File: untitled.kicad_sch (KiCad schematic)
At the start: 9 parts, among them J20 Conn_01x04_Socket, J21 Conn_01x02_Socket, U16 LTV-247

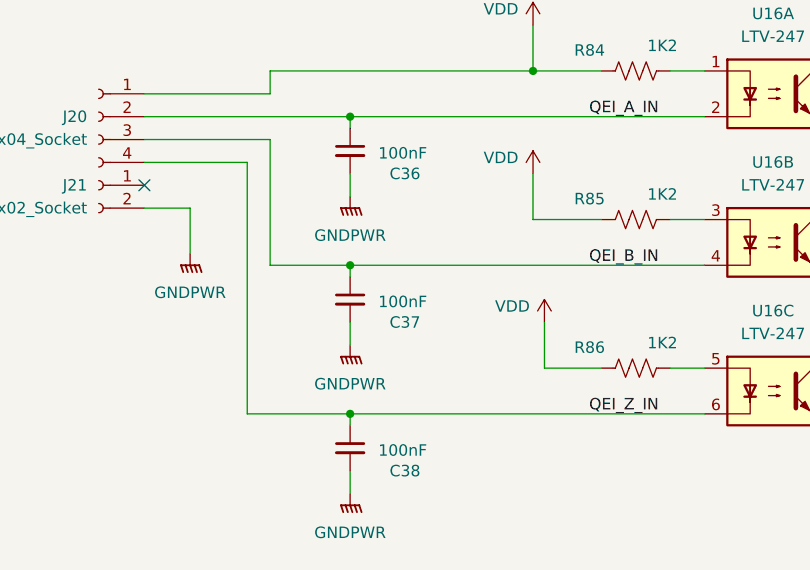
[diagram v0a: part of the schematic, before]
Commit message: Layout for stepper drivers and digital inputs
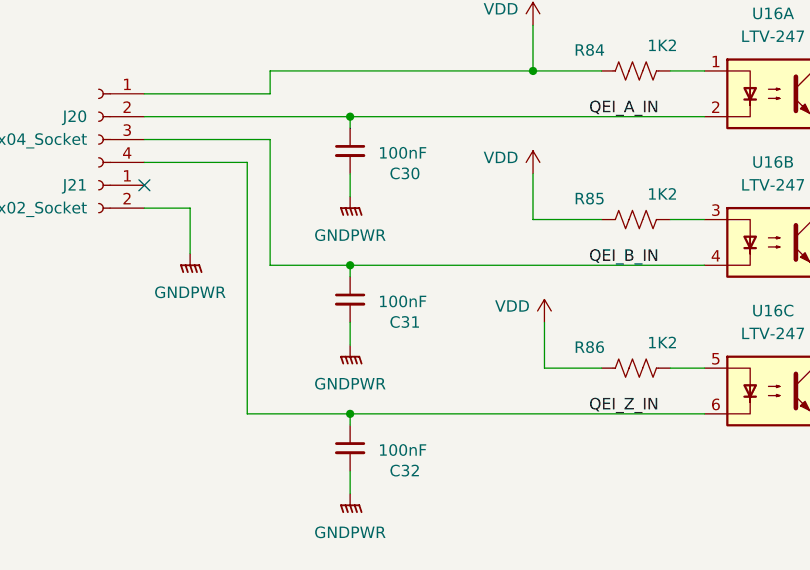
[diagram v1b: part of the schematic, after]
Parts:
- renumbered C36 to C30, C37 to C31, C38 to C32
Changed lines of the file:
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@@
 		(on_board yes)
 		(dnp no)
-		(property "Reference" "#PWR0228"
+		(property "Reference" "#PWR0203"
 			(at 138.43 73.66 0)
 			(effects
@@
 			(project "Remora Nucleo F446ZE Hat"
 				(path "/5473abc6-7b93-43cc-a401-f691c4d7d7cf/e401cb00-fa11-4a99-9e35-1d19f69fa4a0"
-					(reference "#PWR0228")
+					(reference "#PWR0203")
 					(unit 1)
 				)
@@
 		(on_board yes)
 		(dnp no)
-		(property "Reference" "C38"
+		(property "Reference" "C32"
 			(at 124.206 119.38 0)
 			(effects
@@
 			(project "Remora Nucleo F446ZE Hat"
 				(path "/5473abc6-7b93-43cc-a401-f691c4d7d7cf/e401cb00-fa11-4a99-9e35-1d19f69fa4a0"
-					(reference "C38")
+					(reference "C32")
 					(unit 1)
 				)
@@
 		(on_board yes)
 		(dnp no)
-		(property "Reference" "#PWR0229"
+		(property "Reference" "#PWR0204"
 			(at 138.43 90.17 0)
 			(effects
@@
 			(project "Remora Nucleo F446ZE Hat"
 				(path "/5473abc6-7b93-43cc-a401-f691c4d7d7cf/e401cb00-fa11-4a99-9e35-1d19f69fa4a0"
-					(reference "#PWR0229")
+					(reference "#PWR0204")
 					(unit 1)
 				)
@@
 		(on_board yes)
 		(dnp no)
-		(property "Reference" "C37"
+		(property "Reference" "C31"
 			(at 124.206 102.87 0)
 			(effects
@@
 			(project "Remora Nucleo F446ZE Hat"
 				(path "/5473abc6-7b93-43cc-a401-f691c4d7d7cf/e401cb00-fa11-4a99-9e35-1d19f69fa4a0"
-					(reference "C37")
+					(reference "C31")
 					(unit 1)
 				)
@@
 		(on_board yes)
 		(dnp no)
-		(property "Reference" "#PWR0230"
+		(property "Reference" "#PWR0205"
 			(at 139.7 106.68 0)
 			(effects
@@
 			(project "Remora Nucleo F446ZE Hat"
 				(path "/5473abc6-7b93-43cc-a401-f691c4d7d7cf/e401cb00-fa11-4a99-9e35-1d19f69fa4a0"
-					(reference "#PWR0230")
+					(reference "#PWR0205")
 					(unit 1)
 				)
@@
 		(on_board yes)
 		(dnp no)
-		(property "Reference" "C36"
+		(property "Reference" "C30"
 			(at 124.206 86.36 0)
 			(effects
@@
 			(project "Remora Nucleo F446ZE Hat"
 				(path "/5473abc6-7b93-43cc-a401-f691c4d7d7cf/e401cb00-fa11-4a99-9e35-1d19f69fa4a0"
-					(reference "C36")
+					(reference "C30")
 					(unit 1)
 				)
@@
 		(dnp no)
 		(fields_autoplaced yes)
-		(property "Reference" "#PWR0203"
+		(property "Reference" "#PWR0206"
 			(at 193.04 128.27 0)
 			(effects
@@
 			(project "Remora Nucleo F446ZE Hat"
 				(path "/5473abc6-7b93-43cc-a401-f691c4d7d7cf/e401cb00-fa11-4a99-9e35-1d19f69fa4a0"
-					(reference "#PWR0203")
-					(unit 1)
-				)
+					(reference "#PWR0206")
+					(unit 1)
+				)

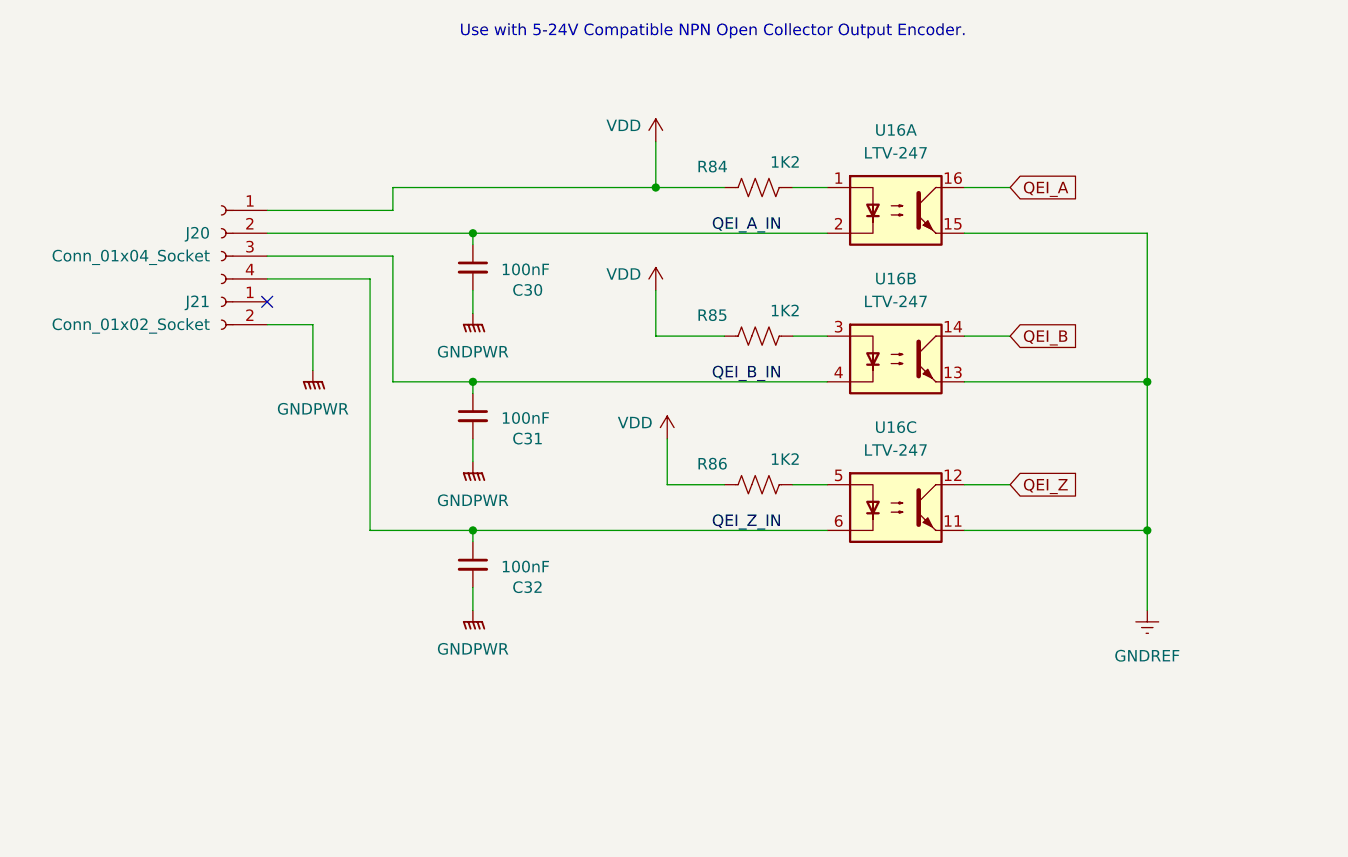
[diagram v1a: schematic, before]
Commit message: Switched terminal footprints over to a finer pitch. Corrected an issue with component reference values preventing proper use of multi channel rule areas. Component references for 4 channel optos are more straightforward as a result
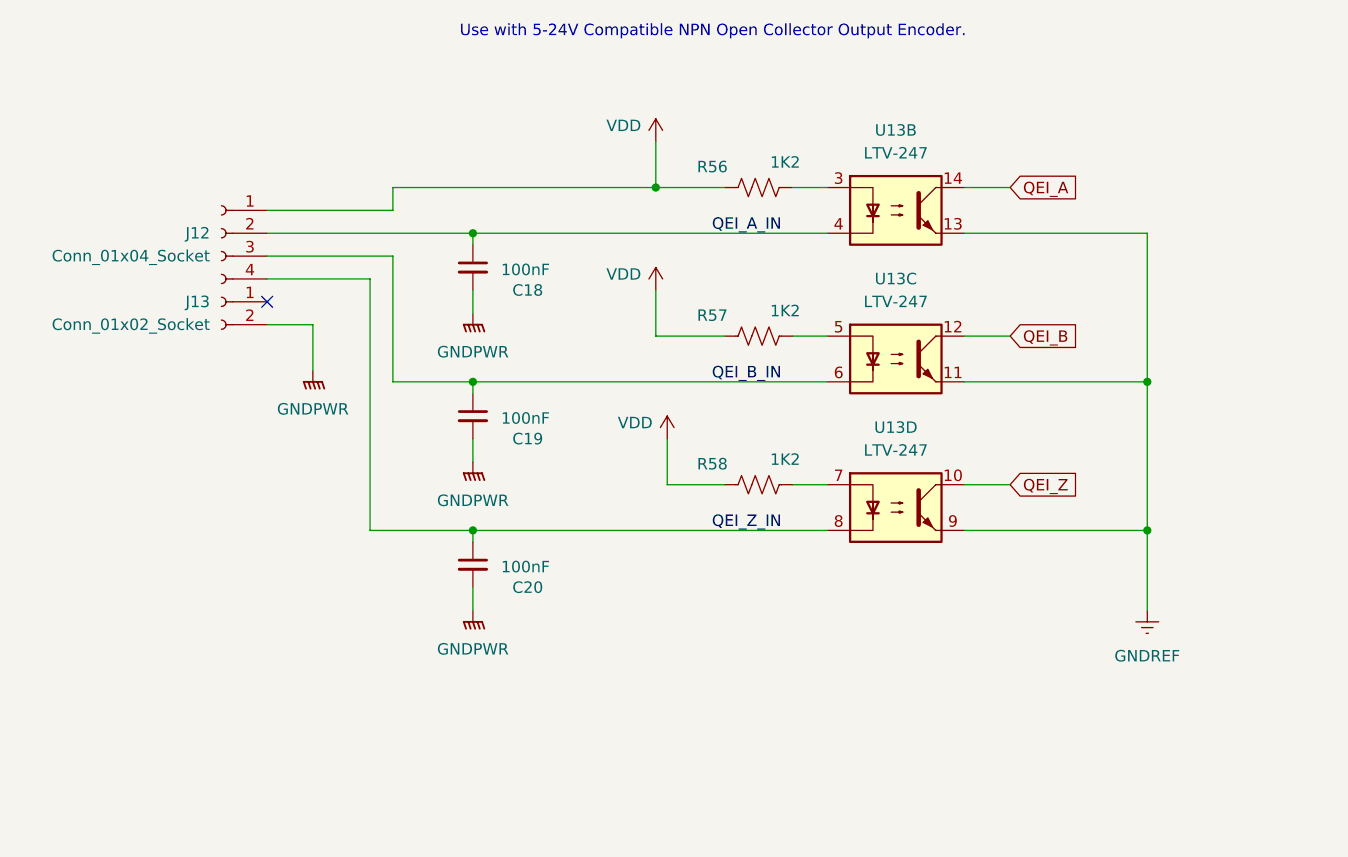
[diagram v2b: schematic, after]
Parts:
- removed U16: LTV-247, Package_SO:SOP-16_4.4x10.4mm_P1.27mm, symbol Isolator:LTV-247
- added U13: LTV-247, Package_SO:SOP-16_4.4x10.4mm_P1.27mm, symbol Isolator:LTV-247
- J12: renamed from J20; footprint Amphenol QT:QT04ADP83V0000G -> 691412120004B:691412120004B; Digikey Part Number 1818-QT04ADP83V0000G-ND -> 732-691412120004B-ND; Digikey URL https://www.digikey.com.au/en/products/detail/amphenol-anyt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 -> https://www.digikey.com.au/en/products/detail/w%C3%BCrth-el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
- J13: renamed from J21; footprint Amphenol QT:QT02ADP83V0000G -> 691412120002B:691412120002B; Digikey Part Number 1818-QT02ADP83V0000G-ND -> 732-691412120002B-ND; Digikey URL https://www.digikey.com.au/en/products/detail/amphenol-anyt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 -> https://www.digikey.com.au/en/products/detail/w%C3%BCrth-el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
- renumbered C30 to C18, C31 to C19, C32 to C20, R84 to R56, R85 to R57, R86 to R58
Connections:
- net GNDREF: now also U13.11, U13.13, U13.9
- net QEI_A: now also U13.14
- net QEI_A_IN: now also U13.4
- net QEI_B: now also U13.12
- net QEI_B_IN: now also U13.6
- net QEI_Z: now also U13.10
- net QEI_Z_IN: now also U13.8
- net at R57.1: now also U13.5
- net at R58.1: now also U13.7
- net at R56.1: now also U13.3

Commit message: Added 3d Models for new terminal connectors for easy board verification before committing to build
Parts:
- renumbered C18 to C30, C19 to C31, C20 to C32, J12 to J20, J13 to J21, R56 to R88, R57 to R89, R58 to R90, U13 to U17
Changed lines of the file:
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@@
 		(dnp no)
 		(fields_autoplaced yes)
-		(property "Reference" "J12"
+		(property "Reference" "J20"
 			(at 88.9 80.0099 0)
 			(effects
@@
 			(project "Remora Nucleo F446ZE Hat"
 				(path "/5473abc6-7b93-43cc-a401-f691c4d7d7cf/e401cb00-fa11-4a99-9e35-1d19f69fa4a0"
-					(reference "J12")
+					(reference "J20")
 					(unit 1)
 				)
@@
 		(on_board yes)
 		(dnp no)
-		(property "Reference" "R58"
+		(property "Reference" "R90"
 			(at 143.002 105.664 90)
 			(effects
@@
 			(project "Remora Nucleo F446ZE Hat"
 				(path "/5473abc6-7b93-43cc-a401-f691c4d7d7cf/e401cb00-fa11-4a99-9e35-1d19f69fa4a0"
-					(reference "R58")
+					(reference "R90")
 					(unit 1)
 				)
@@
 		(dnp no)
 		(fields_autoplaced yes)
-		(property "Reference" "U13"
+		(property "Reference" "U17"
 			(at 165.1 68.58 0)
 			(effects
@@
 			(project "Remora Nucleo F446ZE Hat"
 				(path "/5473abc6-7b93-43cc-a401-f691c4d7d7cf/e401cb00-fa11-4a99-9e35-1d19f69fa4a0"
-					(reference "U13")
+					(reference "U17")
 					(unit 2)
 				)
@@
 		(on_board yes)
 		(dnp no)
-		(property "Reference" "#PWR0143"
+		(property "Reference" "#PWR0211"
 			(at 138.43 73.66 0)
 			(effects
@@
 			(project "Remora Nucleo F446ZE Hat"
 				(path "/5473abc6-7b93-43cc-a401-f691c4d7d7cf/e401cb00-fa11-4a99-9e35-1d19f69fa4a0"
-					(reference "#PWR0143")
+					(reference "#PWR0211")
 					(unit 1)
 				)
@@
 		(on_board yes)
 		(dnp no)
-		(property "Reference" "C20"
+		(property "Reference" "C32"
 			(at 124.206 119.38 0)
 			(effects
@@
 			(project "Remora Nucleo F446ZE Hat"
 				(path "/5473abc6-7b93-43cc-a401-f691c4d7d7cf/e401cb00-fa11-4a99-9e35-1d19f69fa4a0"
-					(reference "C20")
+					(reference "C32")
 					(unit 1)
 				)
@@
 		(dnp no)
 		(fields_autoplaced yes)
-		(property "Reference" "J13"
+		(property "Reference" "J21"
 			(at 88.9 87.6299 0)
 			(effects
@@
 			(project "Remora Nucleo F446ZE Hat"
 				(path "/5473abc6-7b93-43cc-a401-f691c4d7d7cf/e401cb00-fa11-4a99-9e35-1d19f69fa4a0"
-					(reference "J13")
+					(reference "J21")
 					(unit 1)
 				)
@@
 		(on_board yes)
 		(dnp no)
-		(property "Reference" "#PWR0144"
+		(property "Reference" "#PWR0212"
 			(at 138.43 90.17 0)
 			(effects
@@
 			(project "Remora Nucleo F446ZE Hat"
 				(path "/5473abc6-7b93-43cc-a401-f691c4d7d7cf/e401cb00-fa11-4a99-9e35-1d19f69fa4a0"
-					(reference "#PWR0144")
+					(reference "#PWR0212")
 					(unit 1)
 				)
@@
 		(on_board no)
 		(dnp no)
-		(property "Reference" "#PWR0140"
+		(property "Reference" "#PWR0208"
 			(at 118.11 93.98 0)
 			(effects
@@
 			(project "Remora Nucleo F446ZE Hat"
 				(path "/5473abc6-7b93-43cc-a401-f691c4d7d7cf/e401cb00-fa11-4a99-9e35-1d19f69fa4a0"
-					(reference "#PWR0140")
+					(reference "#PWR0208")
 					(unit 1)
 				)
@@
 		(on_board yes)
 		(dnp no)
-		(property "Reference" "C19"
+		(property "Reference" "C31"
 			(at 124.206 102.87 0)
 			(effects
@@
 			(project "Remora Nucleo F446ZE Hat"
 				(path "/5473abc6-7b93-43cc-a401-f691c4d7d7cf/e401cb00-fa11-4a99-9e35-1d19f69fa4a0"
-					(reference "C19")
+					(reference "C31")
 					(unit 1)
 				)
@@
 		(dnp no)
 		(fields_autoplaced yes)
-		(property "Reference" "U13"
+		(property "Reference" "U17"
 			(at 165.1 101.6 0)
 			(effects
@@
 			(project "Remora Nucleo F446ZE Hat"
 				(path "/5473abc6-7b93-43cc-a401-f691c4d7d7cf/e401cb00-fa11-4a99-9e35-1d19f69fa4a0"
-					(reference "U13")
+					(reference "U17")
 					(unit 4)
 				)
@@
 		(on_board yes)
 		(dnp no)
-		(property "Reference" "#PWR0145"
+		(property "Reference" "#PWR0213"
 			(at 139.7 106.68 0)
 			(effects
@@
 			(project "Remora Nucleo F446ZE Hat"
 				(path "/5473abc6-7b93-43cc-a401-f691c4d7d7cf/e401cb00-fa11-4a99-9e35-1d19f69fa4a0"
-					(reference "#PWR0145")
+					(reference "#PWR0213")
 					(unit 1)
 				)
@@
 		(on_board yes)
 		(dnp no)
-		(property "Reference" "R57"
+		(property "Reference" "R89"
 			(at 143.002 89.154 90)
 			(effects
@@
 			(project "Remora Nucleo F446ZE Hat"
 				(path "/5473abc6-7b93-43cc-a401-f691c4d7d7cf/e401cb00-fa11-4a99-9e35-1d19f69fa4a0"
-					(reference "R57")
+					(reference "R89")
 					(unit 1)
 				)
@@
 		(dnp no)
 		(fields_autoplaced yes)
-		(property "Reference" "U13"
+		(property "Reference" "U17"
 			(at 165.1 85.09 0)
 			(effects
@@
 			(project "Remora Nucleo F446ZE Hat"
 				(path "/5473abc6-7b93-43cc-a401-f691c4d7d7cf/e401cb00-fa11-4a99-9e35-1d19f69fa4a0"
-					(reference "U13")
+					(reference "U17")
 					(unit 3)
 				)
@@
 		(on_board no)
 		(dnp no)
-		(property "Reference" "#PWR0139"
+		(property "Reference" "#PWR0207"
 			(at 100.33 100.33 0)
 			(effects
@@
 			(project "Remora Nucleo F446ZE Hat"
 				(path "/5473abc6-7b93-43cc-a401-f691c4d7d7cf/e401cb00-fa11-4a99-9e35-1d19f69fa4a0"
-					(reference "#PWR0139")
+					(reference "#PWR0207")
 					(unit 1)
 				)
@@
 		(on_board yes)
 		(dnp no)
-		(property "Reference" "C18"
+		(property "Reference" "C30"
 			(at 124.206 86.36 0)
 			(effects
@@
 			(project "Remora Nucleo F446ZE Hat"
 				(path "/5473abc6-7b93-43cc-a401-f691c4d7d7cf/e401cb00-fa11-4a99-9e35-1d19f69fa4a0"
-					(reference "C18")
+					(reference "C30")
 					(unit 1)
 				)
@@
 		(on_board no)
 		(dnp no)
-		(property "Reference" "#PWR0142"
+		(property "Reference" "#PWR0210"
 			(at 118.11 127 0)
 			(effects
@@
 			(project "Remora Nucleo F446ZE Hat"
 				(path "/5473abc6-7b93-43cc-a401-f691c4d7d7cf/e401cb00-fa11-4a99-9e35-1d19f69fa4a0"
-					(reference "#PWR0142")
+					(reference "#PWR0210")
 					(unit 1)
 				)
@@
 		(dnp no)
 		(fields_autoplaced yes)
-		(property "Reference" "#PWR0146"
+		(property "Reference" "#PWR0214"
 			(at 193.04 128.27 0)
 			(effects
@@
 			(project "Remora Nucleo F446ZE Hat"
 				(path "/5473abc6-7b93-43cc-a401-f691c4d7d7cf/e401cb00-fa11-4a99-9e35-1d19f69fa4a0"
-					(reference "#PWR0146")
+					(reference "#PWR0214")
 					(unit 1)
 				)
@@
 		(on_board no)
 		(dnp no)
-		(property "Reference" "#PWR0141"
+		(property "Reference" "#PWR0209"
 			(at 118.11 110.49 0)
 			(effects
@@
 			(project "Remora Nucleo F446ZE Hat"
 				(path "/5473abc6-7b93-43cc-a401-f691c4d7d7cf/e401cb00-fa11-4a99-9e35-1d19f69fa4a0"
-					(reference "#PWR0141")
+					(reference "#PWR0209")
 					(unit 1)
 				)
@@
 		(on_board yes)
 		(dnp no)
-		(property "Reference" "R56"
+		(property "Reference" "R88"
 			(at 143.002 72.644 90)
 			(effects
@@
 			(project "Remora Nucleo F446ZE Hat"
 				(path "/5473abc6-7b93-43cc-a401-f691c4d7d7cf/e401cb00-fa11-4a99-9e35-1d19f69fa4a0"
-					(reference "R56")
-					(unit 1)
-				)
+					(reference "R88")
+					(unit 1)
+				)

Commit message: Caught some errors with spacing of jumpers, did some BOM consolidation and included BOM. Updates to Gerbers to reflect new changes.
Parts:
- U17: Digikey Part Number (none) -> 160-2255-1-ND
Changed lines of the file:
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@@
+			)
+		)
+		(property "Digikey Part Number" "160-2255-1-ND"
+			(at 165.1 77.47 0)
+			(effects
+				(font
+					(size 1.27 1.27)
+				)
 			)
 		)
@@
 			)
 		)
+		(property "Digikey Part Number" "160-2255-1-ND"
+			(at 165.1 110.49 0)
+			(effects
+				(font
+					(size 1.27 1.27)
+				)
+			)
+		)
 		(pin "7"
 		)
@@
 			)
 		)
+		(property "Digikey Part Number" "160-2255-1-ND"
+			(at 165.1 93.98 0)
+			(effects
+				(font
+					(size 1.27 1.27)
+				)
+			)
+		)

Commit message: Some file changes and output new gerbers + BOM and centroid file for PCBWay Order
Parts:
- U17: Digikey URL (none) -> https://www.digikey.com.au/en/products/detail/lite-on-inc/l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
- renumbered R88 to R91, R89 to R92, R90 to R93
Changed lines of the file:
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@@
 		(on_board yes)
 		(dnp no)
-		(property "Reference" "R90"
+		(property "Reference" "R93"
 			(at 143.002 105.664 90)
 			(effects
@@
 			(project "Remora Nucleo F446ZE Hat"
 				(path "/5473abc6-7b93-43cc-a401-f691c4d7d7cf/e401cb00-fa11-4a99-9e35-1d19f69fa4a0"
-					(reference "R90")
+					(reference "R93")
 					(unit 1)
 				)
@@
 					(size 1.27 1.27)
 				)
+				(hide yes)
+			)
+		)
+		(property "Digikey URL" "https://www.digikey.com.au/en/products/detail/lite-on-inc/ltv-247/4307982"
+			(at 165.1 77.47 0)
+			(effects
+				(font
+					(size 1.27 1.27)
+				)
+				(hide yes)
 			)
 		)
@@
 					(size 1.27 1.27)
 				)
+				(hide yes)
+			)
+		)
+		(property "Digikey URL" "https://www.digikey.com.au/en/products/detail/lite-on-inc/ltv-247/4307982"
+			(at 165.1 110.49 0)
+			(effects
+				(font
+					(size 1.27 1.27)
+				)
+				(hide yes)
 			)
 		)
@@
 		(on_board yes)
 		(dnp no)
-		(property "Reference" "R89"
+		(property "Reference" "R92"
 			(at 143.002 89.154 90)
 			(effects
@@
 			(project "Remora Nucleo F446ZE Hat"
 				(path "/5473abc6-7b93-43cc-a401-f691c4d7d7cf/e401cb00-fa11-4a99-9e35-1d19f69fa4a0"
-					(reference "R89")
+					(reference "R92")
 					(unit 1)
 				)
@@
 					(size 1.27 1.27)
 				)
+				(hide yes)
+			)
+		)
+		(property "Digikey URL" "https://www.digikey.com.au/en/products/detail/lite-on-inc/ltv-247/4307982"
+			(at 165.1 93.98 0)
+			(effects
+				(font
+					(size 1.27 1.27)
+				)
+				(hide yes)
 			)
 		)
@@
 		(on_board yes)
 		(dnp no)
-		(property "Reference" "R88"
+		(property "Reference" "R91"
 			(at 143.002 72.644 90)
 			(effects
@@
 			(project "Remora Nucleo F446ZE Hat"
 				(path "/5473abc6-7b93-43cc-a401-f691c4d7d7cf/e401cb00-fa11-4a99-9e35-1d19f69fa4a0"
-					(reference "R88")
+					(reference "R91")
 					(unit 1)
 				)
